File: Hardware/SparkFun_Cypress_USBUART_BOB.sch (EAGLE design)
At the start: 27 parts, among them J3 FTDI_BASICPTH, U1 CY7C65213, U2 MIC5219 3.3V

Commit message: Ready for QC review
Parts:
- added LOGO2: OSHW-LOGOS, SparkFun-Aesthetics:OSHW-LOGOS
- J1: value (none) -> MICROB
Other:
- note added: "Open JP1 if VIO used to set VCCIO; close JP2 if VCCIO is below 2.0V. 5.5V > VCCIO > 1.71V See sfe.io/t481"
- note removed: "JP1 must be fully open if JP2 is to be closed! See sfe.io/t481"
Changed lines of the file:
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@@
 <part name="C1" library="SparkFun-Capacitors" deviceset="2.2UF-10V-20%(0603)" device="" value="2.2uF"/>
 <part name="U2" library="SparkFun-PowerIC" deviceset="V_REG_MIC5219" device="3.3V" value="MIC5219 3.3V"/>
-<part name="J1" library="SparkFun-Connectors" deviceset="USB_MICROB_PLUG" device="CONN-11752"/>
+<part name="J1" library="SparkFun-Connectors" deviceset="USB_MICROB_PLUG" device="CONN-11752" value="MICROB"/>
 <part name="J2" library="SparkFun-Connectors" deviceset="M02" device="PTH"/>
 <part name="J3" library="SparkFun-Connectors" deviceset="FTDI_BASIC" device="PTH"/>
@@
 <part name="C6" library="SparkFun-Capacitors" deviceset="4.7UF-16V-20%,+80%-(1206)" device="" value="4.7uF"/>
 <part name="SUPPLY23" library="SparkFun-Aesthetics" deviceset="VCCIO" device=""/>
+<part name="LOGO2" library="SparkFun-Aesthetics" deviceset="OSHW-LOGO" device="S"/>
 </parts>
 <sheets>
 <sheet>
 <plain>
-<text x="237.998" y="6.35" size="3.81" layer="91" font="vector">01</text>
-<text x="154.432" y="6.096" size="3.81" layer="91" font="vector">Mike Hord</text>
-<text x="27.94" y="99.06" size="1.27" layer="97" font="vector">JP1 must be fully open
-if JP2 is to be closed!
+<text x="237.998" y="6.35" size="3.81" layer="94" font="vector">01</text>
+<text x="154.432" y="6.096" size="3.81" layer="94" font="vector">Mike Hord</text>
+<text x="27.94" y="95.25" size="1.27" layer="97" font="vector">Open JP1 if VIO used
+to set VCCIO; close JP2
+if VCCIO is below 2.0V.
+5.5V &gt; VCCIO &gt; 1.71V
 See sfe.io/t481</text>
 <wire x1="71.12" y1="185.42" x2="71.12" y2="106.68" width="0.3048" layer="97" style="longdash"/>
@@
 <instance part="C1" gate="G$1" x="20.32" y="139.7"/>
 <instance part="U2" gate="G$1" x="35.56" y="76.2"/>
-<instance part="J1" gate="G$1" x="99.06" y="68.58" rot="MR0"/>
+<instance part="J1" gate="G$1" x="99.06" y="68.58" smashed="yes" rot="MR0">
+<attribute name="NAME" x="103.886" y="76.708" size="1.778" layer="95" rot="MR0"/>
+<attribute name="VALUE" x="104.14" y="58.674" size="1.778" layer="96" rot="MR0"/>
+</instance>
 <instance part="J2" gate="G$1" x="200.66" y="81.28"/>
 <instance part="J3" gate="G$1" x="203.2" y="63.5" rot="MR180"/>
@@
 <instance part="C6" gate="G$1" x="60.96" y="147.32"/>
 <instance part="SUPPLY23" gate="G$1" x="50.8" y="160.02"/>
+<instance part="LOGO2" gate="G$1" x="132.08" y="10.16"/>
 </instances>
 <busses>
@@
 <pinref part="J1" gate="G$1" pin="SHIELD"/>
 <wire x1="91.44" y1="68.58" x2="88.9" y2="68.58" width="0.1524" layer="91"/>
-<wire x1="88.9" y1="68.58" x2="88.9" y2="58.42" width="0.1524" layer="91"/>
-<wire x1="88.9" y1="58.42" x2="91.44" y2="58.42" width="0.1524" layer="91"/>
-<label x="91.44" y="58.42" size="1.27" layer="95" font="vector" xref="yes"/>
+<wire x1="88.9" y1="68.58" x2="88.9" y2="55.88" width="0.1524" layer="91"/>
+<wire x1="88.9" y1="55.88" x2="91.44" y2="55.88" width="0.1524" layer="91"/>
+<label x="91.44" y="55.88" size="1.27" layer="95" font="vector" xref="yes"/>
 </segment>
 </net>
@@
 <pinref part="U1" gate="G$1" pin="GPIO5"/>
 <wire x1="147.32" y1="129.54" x2="149.86" y2="129.54" width="0.1524" layer="91" style="longdash"/>
-<label x="149.86" y="129.54" size="1.27" layer="91" font="vector" xref="yes"/>
-</segment>
-</net>
+<label x="149.86" y="129.54" size="1.27" layer="95" font="vector" xref="yes"/>
+</segment>
+</net>

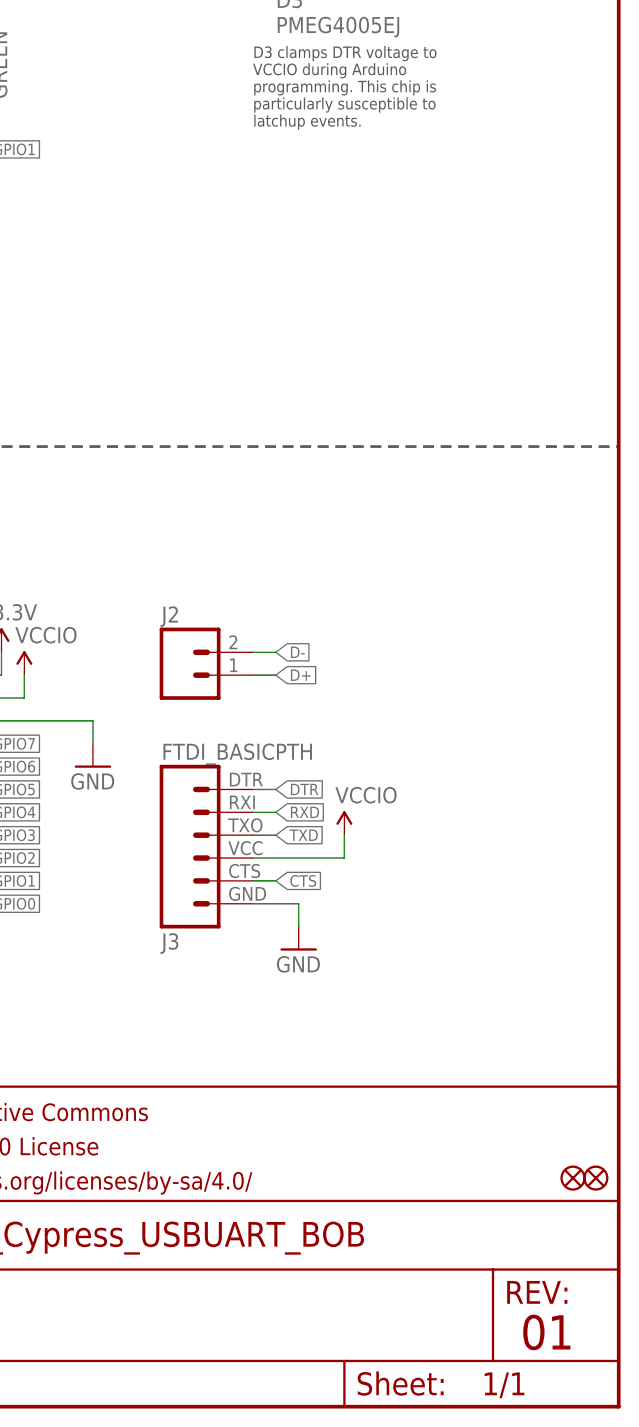
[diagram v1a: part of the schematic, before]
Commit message: Rotate a couple of parts, add 10k resistor, v02
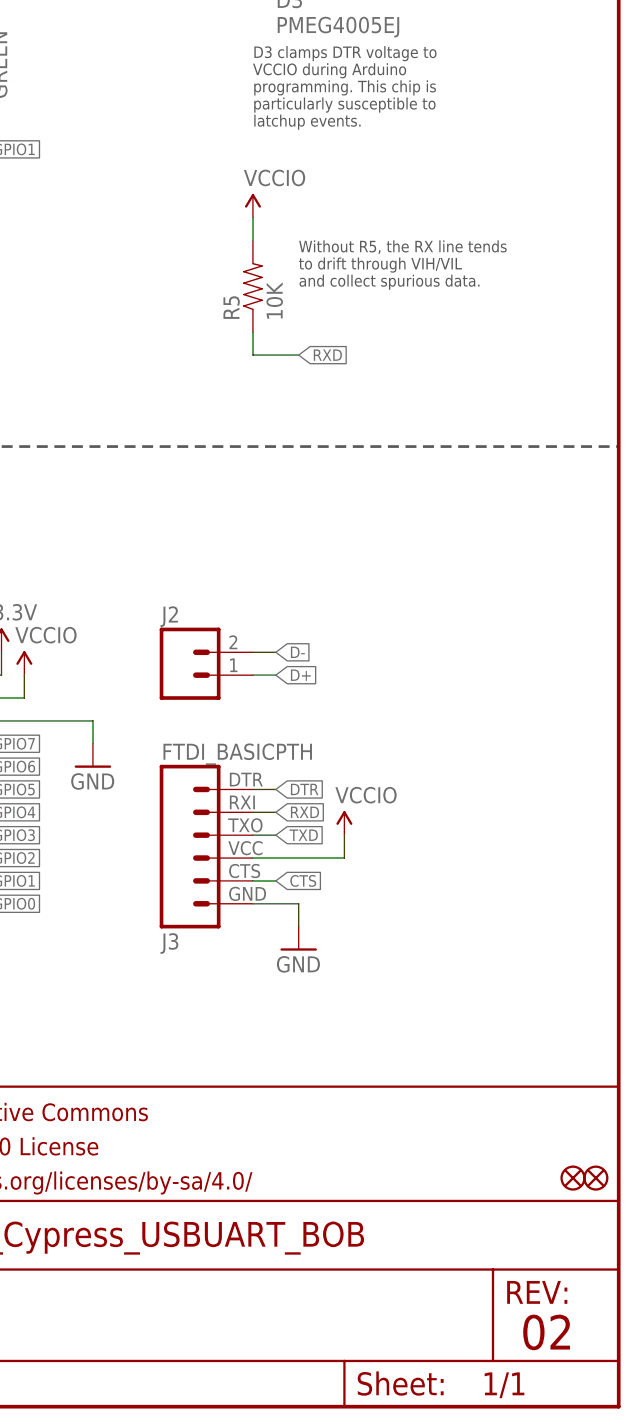
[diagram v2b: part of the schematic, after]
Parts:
- added R5: 10K, SparkFun-Resistors:10KOHM-1/10W-1%(0603)0603
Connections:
- net RXD: now also R5.1
- net VCCIO: now also R5.2
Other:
- note added: "02"
- note added: "Without R5, the RX line tends to drift through VIH/VIL and collect spurious data."
- note removed: "01"
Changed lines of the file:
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@@
 <?xml version="1.0" encoding="utf-8"?>
 <!DOCTYPE eagle SYSTEM "eagle.dtd">
-<eagle version="7.3.0">
+<eagle version="7.5.0">
 <drawing>
 <settings>
@@
 <part name="SUPPLY23" library="SparkFun-Aesthetics" deviceset="VCCIO" device=""/>
 <part name="LOGO2" library="SparkFun-Aesthetics" deviceset="OSHW-LOGO" device="S"/>
+<part name="R5" library="SparkFun-Resistors" deviceset="10KOHM-1/10W-1%(0603)" device="0603" value="10K"/>
+<part name="SUPPLY24" library="SparkFun-Aesthetics" deviceset="VCCIO" device=""/>
 </parts>
 <sheets>
 <sheet>
 <plain>
-<text x="237.998" y="6.35" size="3.81" layer="94" font="vector">01</text>
+<text x="237.998" y="6.35" size="3.81" layer="94" font="vector">02</text>
 <text x="154.432" y="6.096" size="3.81" layer="94" font="vector">Mike Hord</text>
 <text x="27.94" y="95.25" size="1.27" layer="97" font="vector">Open JP1 if VIO used
@@
 may cause spikes on
 5V line.</text>
+<text x="213.36" y="124.46" size="1.27" layer="97" font="vector">Without R5, the RX line tends
+to drift through VIH/VIL
+and collect spurious data.</text>
 </plain>
 <instances>
@@
 <instance part="SUPPLY23" gate="G$1" x="50.8" y="160.02"/>
 <instance part="LOGO2" gate="G$1" x="132.08" y="10.16"/>
+<instance part="R5" gate="G$1" x="208.28" y="124.46" rot="R90"/>
+<instance part="SUPPLY24" gate="G$1" x="208.28" y="132.08"/>
 </instances>
 <busses>
@@
 <junction x="50.8" y="157.48"/>
 </segment>
+<segment>
+<pinref part="SUPPLY24" gate="G$1" pin="VCCIO"/>
+<pinref part="R5" gate="G$1" pin="2"/>
+<wire x1="208.28" y1="132.08" x2="208.28" y2="129.54" width="0.1524" layer="91"/>
+</segment>
 </net>
 <net name="GPIO6" class="0">
@@
 <label x="210.82" y="66.04" size="1.27" layer="95" font="vector" rot="MR180" xref="yes"/>
 </segment>
-</net>
+<segment>
+<pinref part="R5" gate="G$1" pin="1"/>
+<wire x1="208.28" y1="119.38" x2="208.28" y2="116.84" width="0.1524" layer="91"/>
+<wire x1="208.28" y1="116.84" x2="213.36" y2="116.84" width="0.1524" layer="91"/>
+<label x="213.36" y="116.84" size="1.27" layer="95" xref="yes"/>
+</segment>
+</net>
